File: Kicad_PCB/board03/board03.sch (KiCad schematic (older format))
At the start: 7 parts, among them J1 USB_B_Micro, Q1 BF545C, U1 STM32F401CCFx, U2 AMS1117-3.3, U3 tmag5273

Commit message: coil and all
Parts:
- added L1: L_core_v, L_Core_vlv:L_core_v, symbol L_core_valv:L_core_v
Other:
- moved on the sheet: D1, D2, Q1, U3
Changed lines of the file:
@@
 L TMAG5273Hall:tmag5273 U3
 U 1 1 610194D7
-P 3250 6075
-F 0 "U3" H 3200 6550 50  0000 C CNN
-F 1 "tmag5273" H 3200 6459 50  0000 C CNN
-F 2 "Package_TO_SOT_SMD:SOT-23-6" H 3250 6075 50  0001 C CNN
-F 3 "" H 3250 6075 50  0001 C CNN
-	1    3250 6075
+P 9125 4750
+F 0 "U3" H 9075 5225 50  0000 C CNN
+F 1 "tmag5273" H 9075 5134 50  0000 C CNN
+F 2 "Package_TO_SOT_SMD:SOT-23-6" H 9125 4750 50  0001 C CNN
+F 3 "" H 9125 4750 50  0001 C CNN
+	1    9125 4750
 	1    0    0    -1
 $EndComp
@@
 L Transistor_FET:BF545C Q1
 U 1 1 61032CC8
-P 3750 3050
-F 0 "Q1" H 3940 3096 50  0000 L CNN
-F 1 "BF545C" H 3940 3005 50  0000 L CNN
-F 2 "Package_TO_SOT_SMD:SOT-23" H 3950 2975 50  0001 L CIN
-F 3 "https://www.nxp.com/docs/en/data-sheet/BF545A_BF545B_BF545C.pdf" H 3750 3050 50  0001 L CNN
-	1    3750 3050
+P 7425 3200
+F 0 "Q1" H 7615 3246 50  0000 L CNN
+F 1 "BF545C" H 7615 3155 50  0000 L CNN
+F 2 "Package_TO_SOT_SMD:SOT-23" H 7625 3125 50  0001 L CIN
+F 3 "https://www.nxp.com/docs/en/data-sheet/BF545A_BF545B_BF545C.pdf" H 7425 3200 50  0001 L CNN
+	1    7425 3200
 	1    0    0    -1
 $EndComp
@@
 L dk_LED-Indication-Discrete:LH_R974-LP-1 D1
 U 1 1 6103E8C0
-P 7800 3275
-F 0 "D1" H 7750 3612 60  0000 C CNN
-F 1 "LH_R974-LP-1" H 7750 3506 60  0000 C CNN
-F 2 "LED_SMD:LED_0805_2012Metric" H 8000 3475 60  0001 L CNN
-F 3 "https://dammedia.osram.info/media/resource/hires/osram-dam-2493888/LH%20R974.pdf" H 8000 3575 60  0001 L CNN
-F 4 "475-1415-1-ND" H 8000 3675 60  0001 L CNN "Digi-Key_PN"
-F 5 "LH R974-LP-1" H 8000 3775 60  0001 L CNN "MPN"
-F 6 "Optoelectronics" H 8000 3875 60  0001 L CNN "Category"
-F 7 "LED Indication - Discrete" H 8000 3975 60  0001 L CNN "Family"
-F 8 "https://dammedia.osram.info/media/resource/hires/osram-dam-2493888/LH%20R974.pdf" H 8000 4075 60  0001 L CNN "DK_Datasheet_Link"
-F 9 "/product-detail/en/osram-opto-semiconductors-inc/LH-R974-LP-1/475-1415-1-ND/1802604" H 8000 4175 60  0001 L CNN "DK_Detail_Page"
-F 10 "LED RED DIFFUSED 0805 SMD" H 8000 4275 60  0001 L CNN "Description"
-F 11 "OSRAM Opto Semiconductors Inc." H 8000 4375 60  0001 L CNN "Manufacturer"
-F 12 "Active" H 8000 4475 60  0001 L CNN "Status"
-	1    7800 3275
+P 9050 2725
+F 0 "D1" H 9000 3062 60  0000 C CNN
+F 1 "LH_R974-LP-1" H 9000 2956 60  0000 C CNN
+F 2 "LED_SMD:LED_0805_2012Metric" H 9250 2925 60  0001 L CNN
+F 3 "https://dammedia.osram.info/media/resource/hires/osram-dam-2493888/LH%20R974.pdf" H 9250 3025 60  0001 L CNN
+F 4 "475-1415-1-ND" H 9250 3125 60  0001 L CNN "Digi-Key_PN"
+F 5 "LH R974-LP-1" H 9250 3225 60  0001 L CNN "MPN"
+F 6 "Optoelectronics" H 9250 3325 60  0001 L CNN "Category"
+F 7 "LED Indication - Discrete" H 9250 3425 60  0001 L CNN "Family"
+F 8 "https://dammedia.osram.info/media/resource/hires/osram-dam-2493888/LH%20R974.pdf" H 9250 3525 60  0001 L CNN "DK_Datasheet_Link"
+F 9 "/product-detail/en/osram-opto-semiconductors-inc/LH-R974-LP-1/475-1415-1-ND/1802604" H 9250 3625 60  0001 L CNN "DK_Detail_Page"
+F 10 "LED RED DIFFUSED 0805 SMD" H 9250 3725 60  0001 L CNN "Description"
+F 11 "OSRAM Opto Semiconductors Inc." H 9250 3825 60  0001 L CNN "Manufacturer"
+F 12 "Active" H 9250 3925 60  0001 L CNN "Status"
+	1    9050 2725
 	1    0    0    -1
 $EndComp
@@
 L dk_LED-Indication-Discrete:LG_R971-KN-1 D2
 U 1 1 61040C00
-P 7775 3850
-F 0 "D2" H 7725 4187 60  0000 C CNN
-F 1 "LG_R971-KN-1" H 7725 4081 60  0000 C CNN
-F 2 "LED_SMD:LED_0805_2012Metric" H 7975 4050 60  0001 L CNN
-F 3 "https://dammedia.osram.info/media/resource/hires/osram-dam-2493936/LG%20R971.pdf" H 7975 4150 60  0001 L CNN
-F 4 "475-1410-1-ND" H 7975 4250 60  0001 L CNN "Digi-Key_PN"
-F 5 "LG R971-KN-1" H 7975 4350 60  0001 L CNN "MPN"
-F 6 "Optoelectronics" H 7975 4450 60  0001 L CNN "Category"
-F 7 "LED Indication - Discrete" H 7975 4550 60  0001 L CNN "Family"
-F 8 "https://dammedia.osram.info/media/resource/hires/osram-dam-2493936/LG%20R971.pdf" H 7975 4650 60  0001 L CNN "DK_Datasheet_Link"
-F 9 "/product-detail/en/osram-opto-semiconductors-inc/LG-R971-KN-1/475-1410-1-ND/1802598" H 7975 4750 60  0001 L CNN "DK_Detail_Page"
-F 10 "LED GREEN DIFFUSED 0805 SMD" H 7975 4850 60  0001 L CNN "Description"
-F 11 "OSRAM Opto Semiconductors Inc." H 7975 4950 60  0001 L CNN "Manufacturer"
-F 12 "Active" H 7975 5050 60  0001 L CNN "Status"
-	1    7775 3850
+P 9025 3300
+F 0 "D2" H 8975 3637 60  0000 C CNN
+F 1 "LG_R971-KN-1" H 8975 3531 60  0000 C CNN
+F 2 "LED_SMD:LED_0805_2012Metric" H 9225 3500 60  0001 L CNN
+F 3 "https://dammedia.osram.info/media/resource/hires/osram-dam-2493936/LG%20R971.pdf" H 9225 3600 60  0001 L CNN
+F 4 "475-1410-1-ND" H 9225 3700 60  0001 L CNN "Digi-Key_PN"
+F 5 "LG R971-KN-1" H 9225 3800 60  0001 L CNN "MPN"
+F 6 "Optoelectronics" H 9225 3900 60  0001 L CNN "Category"
+F 7 "LED Indication - Discrete" H 9225 4000 60  0001 L CNN "Family"
+F 8 "https://dammedia.osram.info/media/resource/hires/osram-dam-2493936/LG%20R971.pdf" H 9225 4100 60  0001 L CNN "DK_Datasheet_Link"
+F 9 "/product-detail/en/osram-opto-semiconductors-inc/LG-R971-KN-1/475-1410-1-ND/1802598" H 9225 4200 60  0001 L CNN "DK_Detail_Page"
+F 10 "LED GREEN DIFFUSED 0805 SMD" H 9225 4300 60  0001 L CNN "Description"
+F 11 "OSRAM Opto Semiconductors Inc." H 9225 4400 60  0001 L CNN "Manufacturer"
+F 12 "Active" H 9225 4500 60  0001 L CNN "Status"
+	1    9025 3300
 	1    0    0    -1
 $EndComp
+$Comp
+L L_core_valv:L_core_v L1
+U 1 1 61045340
+P 7400 4375
+F 0 "L1" H 7736 4433 50  0000 L CNN
+F 1 "L_core_v" H 7736 4342 50  0000 L CNN
+F 2 "L_Core_vlv:L_core_v" H 7400 4375 50  0001 C CNN
+F 3 "" H 7400 4375 50  0001 C CNN
+	1    7400 4375
+	1    0    0    -1
+$EndComp

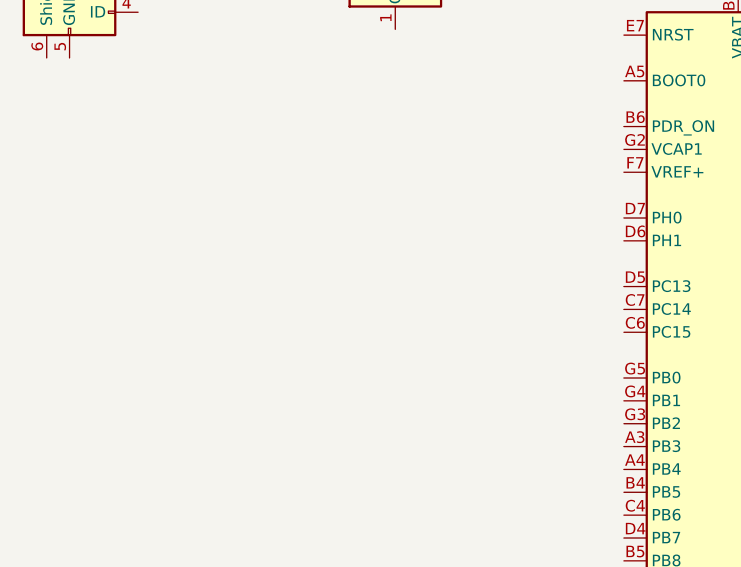
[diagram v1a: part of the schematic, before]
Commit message: cap toch sensor
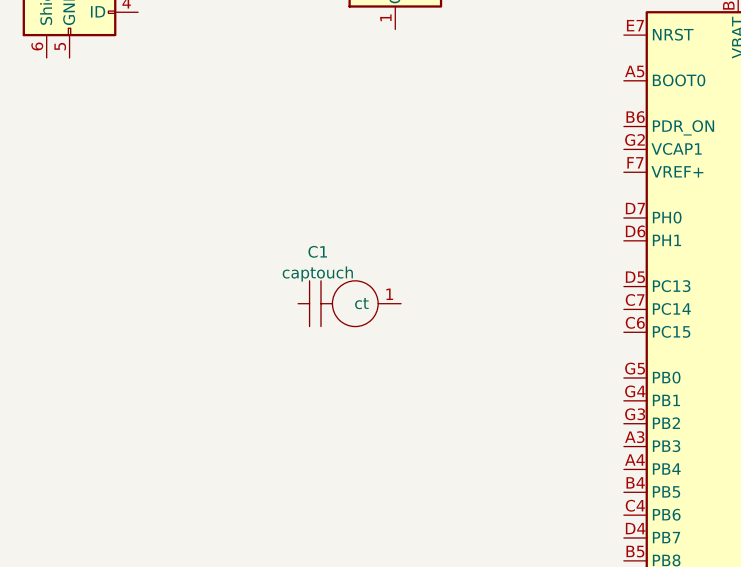
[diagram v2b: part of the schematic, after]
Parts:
- added C1: captouch, cap_touch:capS, symbol cup_touch:captouch
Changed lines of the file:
@@
 	1    0    0    -1
 $EndComp
+$Comp
+L cup_touch:captouch C1
+U 1 1 61056B2A
+P 3850 3450
+F 0 "C1" H 3863 3675 50  0000 C CNN
+F 1 "captouch" H 3863 3584 50  0000 C CNN
+F 2 "cap_touch:capS" H 3950 3300 50  0001 C CNN
+F 3 "" H 3850 3450 50  0001 C CNN
+	1    3850 3450
+	-1   0    0    -1
+$EndComp
 $EndSCHEMATC

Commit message: sensor Vlt
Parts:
- added U4: sensV, sensorVlt:SensV, symbol sens_vlt:sensV
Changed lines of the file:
@@
 U 1 1 61045340
 P 7400 4375
-F 0 "L1" H 7736 4433 50  0000 L CNN
-F 1 "L_core_v" H 7736 4342 50  0000 L CNN
+F 0 "L1" H 7425 4100 50  0000 L CNN
+F 1 "L_core_v" H 7400 4700 50  0000 L CNN
 F 2 "L_Core_vlv:L_core_v" H 7400 4375 50  0001 C CNN
 F 3 "" H 7400 4375 50  0001 C CNN
@@
 	-1   0    0    -1
 $EndComp
+$Comp
+L sens_vlt:sensV U4
+U 1 1 61059F3E
+P 3925 4150
+F 0 "U4" H 3883 4425 50  0000 C CNN
+F 1 "sensV" H 3883 4334 50  0000 C CNN
+F 2 "sensorVlt:SensV" H 3925 4150 50  0001 C CNN
+F 3 "" H 3925 4150 50  0001 C CNN
+	1    3925 4150
+	1    0    0    -1
+$EndComp
 $EndSCHEMATC
